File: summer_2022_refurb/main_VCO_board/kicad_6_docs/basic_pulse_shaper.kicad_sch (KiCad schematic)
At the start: 11 parts

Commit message: Main VCO progress
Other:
- title: (none) -> Josh Ox Ribon Synth Main VCO board
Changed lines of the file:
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@@
 (kicad_sch (version 20211123) (generator eeschema)
   (paper "A4")
+  (title_block
+    (title "Josh Ox Ribon Synth Main VCO board")
+    (date "2022-06-18")
+    (rev "0")
+    (comment 2 "creativecommons.org/licences/by/4.0")
+    (comment 3 "license: CC by 4.0")
+    (comment 4 "Author: Jordan Acete")
+  )
   (junction (at 121.92 118.11) (diameter 0) (color 0 0 0 0)
   )

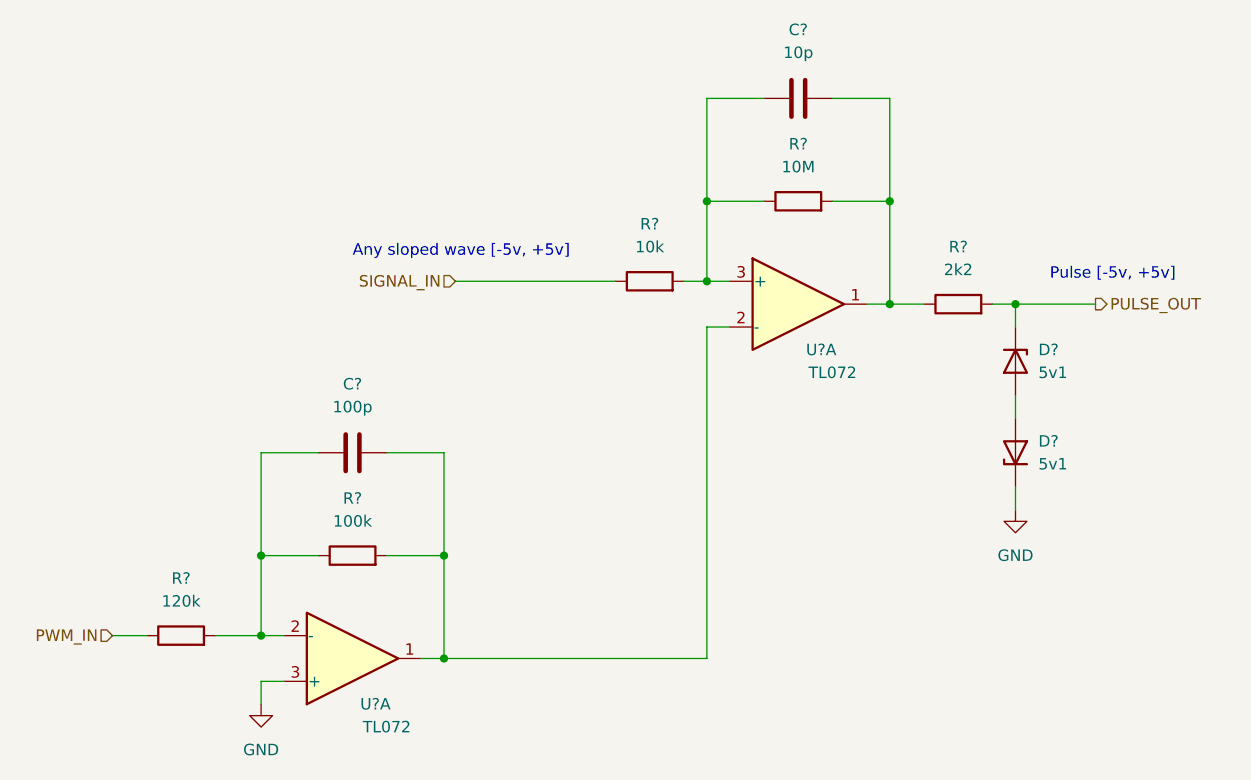
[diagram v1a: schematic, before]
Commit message: Progress on main VCO, schem getting close but not done
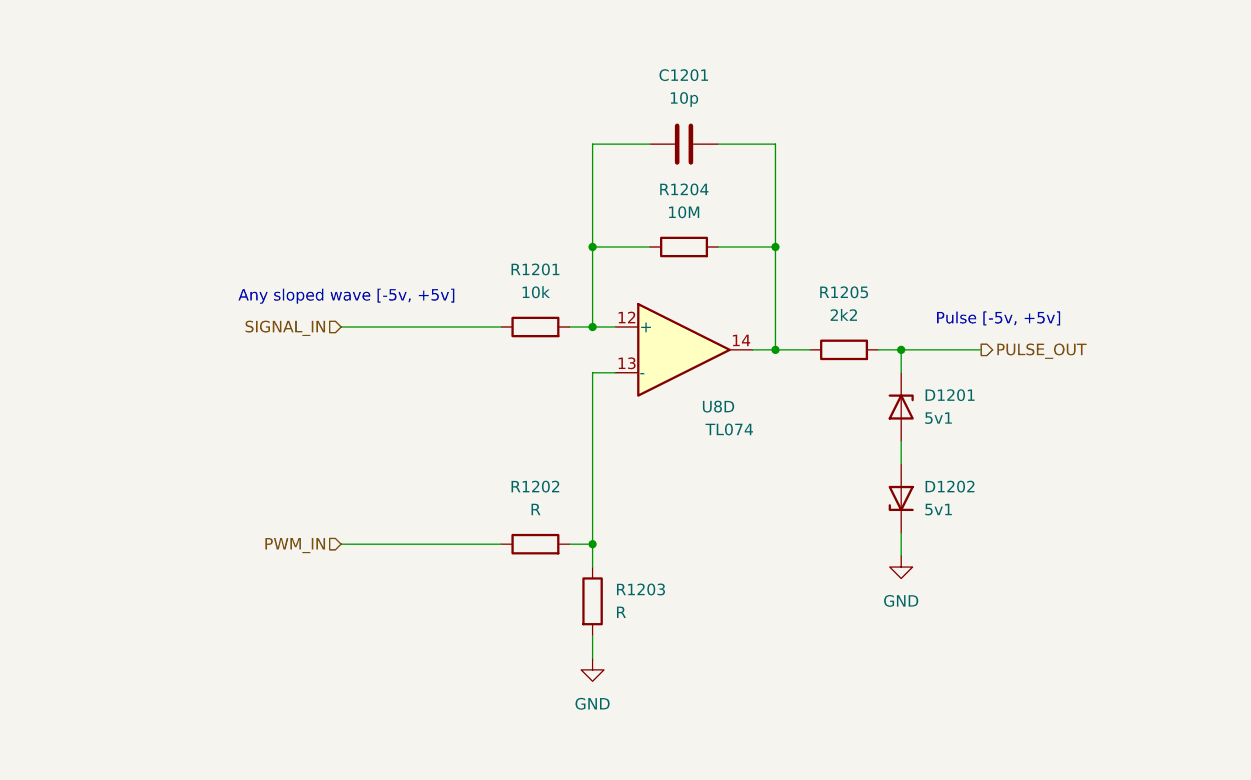
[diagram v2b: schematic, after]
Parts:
- removed C?: 100p, symbol Device:C
- removed R?: 120k, symbol Device:R
- removed R?: 100k, symbol Device:R
- removed U? (x2): TL072, symbol Amplifier_Operational:TL072
- added R1202, R1203: R, symbol Device:R
- added U8: TL074, symbol Amplifier_Operational:TL074
- gave numbers to parts that had none: 6
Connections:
- net GND: now also R1203.2
- net PWM_IN: now also R1202.1
- net at C1201.1, R1201.2, R1204.1: now also U8.12 (+)
- net at C1201.2, R1204.2, R1205.1: now also U8.14
- new net: R1202.2, R1203.1, U8.13 (-)
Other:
- moved on the sheet: C1201, D1201, D1202, R1201, R1204, R1205

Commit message: Main VCO rough parts placement
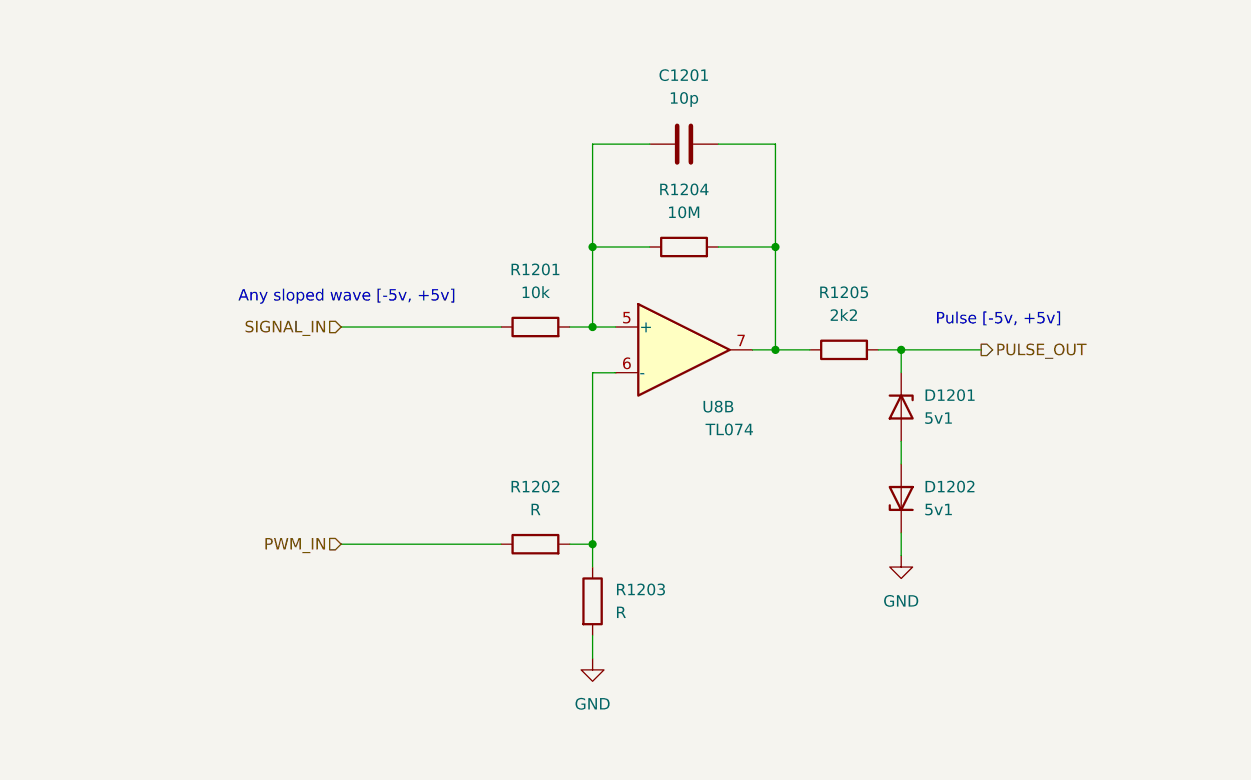
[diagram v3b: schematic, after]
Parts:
- C1201: footprint (none) -> Capacitor_SMD:C_0805_2012Metric
- D1201, D1202: footprint (none) -> Diode_SMD:D_SOD-123
- R1201, R1202, R1203, R1204, R1205: footprint (none) -> Resistor_SMD:R_0805_2012Metric
- U8: footprint (none) -> Package_SO:SOIC-14_3.9x8.7mm_P1.27mm
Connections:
- net at C1201.1, R1201.2, R1204.1: now also U8.5 (+); no longer U8.12 (+)
- net at C1201.2, R1204.2, R1205.1: now also U8.7; no longer U8.14
- net at R1202.2, R1203.1: now also U8.6 (-); no longer U8.13 (-)
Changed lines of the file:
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@@
     (property "Reference" "R1201" (id 0) (at 132.08 86.36 90))
     (property "Value" "10k" (id 1) (at 132.08 88.9 90))
-    (property "Footprint" "" (id 2) (at 132.08 94.488 90)
+    (property "Footprint" "Resistor_SMD:R_0805_2012Metric" (id 2) (at 132.08 94.488 90)
       (effects (font (size 1.27 1.27)) hide)
     )
@@
     (property "Reference" "R1205" (id 0) (at 166.37 88.9 90))
     (property "Value" "2k2" (id 1) (at 166.37 91.44 90))
-    (property "Footprint" "" (id 2) (at 166.37 97.028 90)
+    (property "Footprint" "Resistor_SMD:R_0805_2012Metric" (id 2) (at 166.37 97.028 90)
       (effects (font (size 1.27 1.27)) hide)
     )
@@
     (property "Reference" "C1201" (id 0) (at 148.59 64.77 90))
     (property "Value" "10p" (id 1) (at 148.59 67.31 90))
-    (property "Footprint" "" (id 2) (at 152.4 71.4248 0)
+    (property "Footprint" "Capacitor_SMD:C_0805_2012Metric" (id 2) (at 152.4 71.4248 0)
       (effects (font (size 1.27 1.27)) hide)
     )
@@
     (pin "2")
   )
-  (symbol (lib_id "Amplifier_Operational:TL074") (at 148.59 95.25 0) (unit 4)
+  (symbol (lib_id "Amplifier_Operational:TL074") (at 148.59 95.25 0) (unit 2)
     (in_bom yes) (on_board yes)
     (property "Reference" "U8" (id 0) (at 152.4 101.6 0))
     (property "Value" "TL074" (id 1) (at 153.67 104.14 0))
-    (property "Footprint" "" (id 2) (at 147.32 92.71 0)
+    (property "Footprint" "Package_SO:SOIC-14_3.9x8.7mm_P1.27mm" (id 2) (at 147.32 92.71 0)
       (effects (font (size 1.27 1.27)) hide)
     )
@@
     (property "Reference" "R1202" (id 0) (at 132.08 110.49 90))
     (property "Value" "R" (id 1) (at 132.08 113.03 90))
-    (property "Footprint" "" (id 2) (at 132.08 118.618 90)
+    (property "Footprint" "Resistor_SMD:R_0805_2012Metric" (id 2) (at 132.08 118.618 90)
       (effects (font (size 1.27 1.27)) hide)
     )
@@
     (property "Reference" "R1204" (id 0) (at 148.59 77.47 90))
     (property "Value" "10M" (id 1) (at 148.59 80.01 90))
-    (property "Footprint" "" (id 2) (at 148.59 85.598 90)
+    (property "Footprint" "Resistor_SMD:R_0805_2012Metric" (id 2) (at 148.59 85.598 90)
       (effects (font (size 1.27 1.27)) hide)
     )
@@
       (effects (font (size 1.27 1.27)) (justify left))
     )
-    (property "Footprint" "" (id 2) (at 136.652 123.19 90)
+    (property "Footprint" "Resistor_SMD:R_0805_2012Metric" (id 2) (at 136.652 123.19 90)
       (effects (font (size 1.27 1.27)) hide)
     )
@@
       (effects (font (size 1.27 1.27)) (justify right))
     )
-    (property "Footprint" "" (id 2) (at 172.72 111.76 0)
+    (property "Footprint" "Diode_SMD:D_SOD-123" (id 2) (at 172.72 111.76 0)
       (effects (font (size 1.27 1.27)) hide)
     )
@@
       (effects (font (size 1.27 1.27)) (justify left))
     )
-    (property "Footprint" "" (id 2) (at 172.72 101.6 0)
+    (property "Footprint" "Diode_SMD:D_SOD-123" (id 2) (at 172.72 101.6 0)
       (effects (font (size 1.27 1.27)) hide)
     )
